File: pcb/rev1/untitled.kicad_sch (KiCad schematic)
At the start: 40 parts, among them U7 TL084, U8 TL084

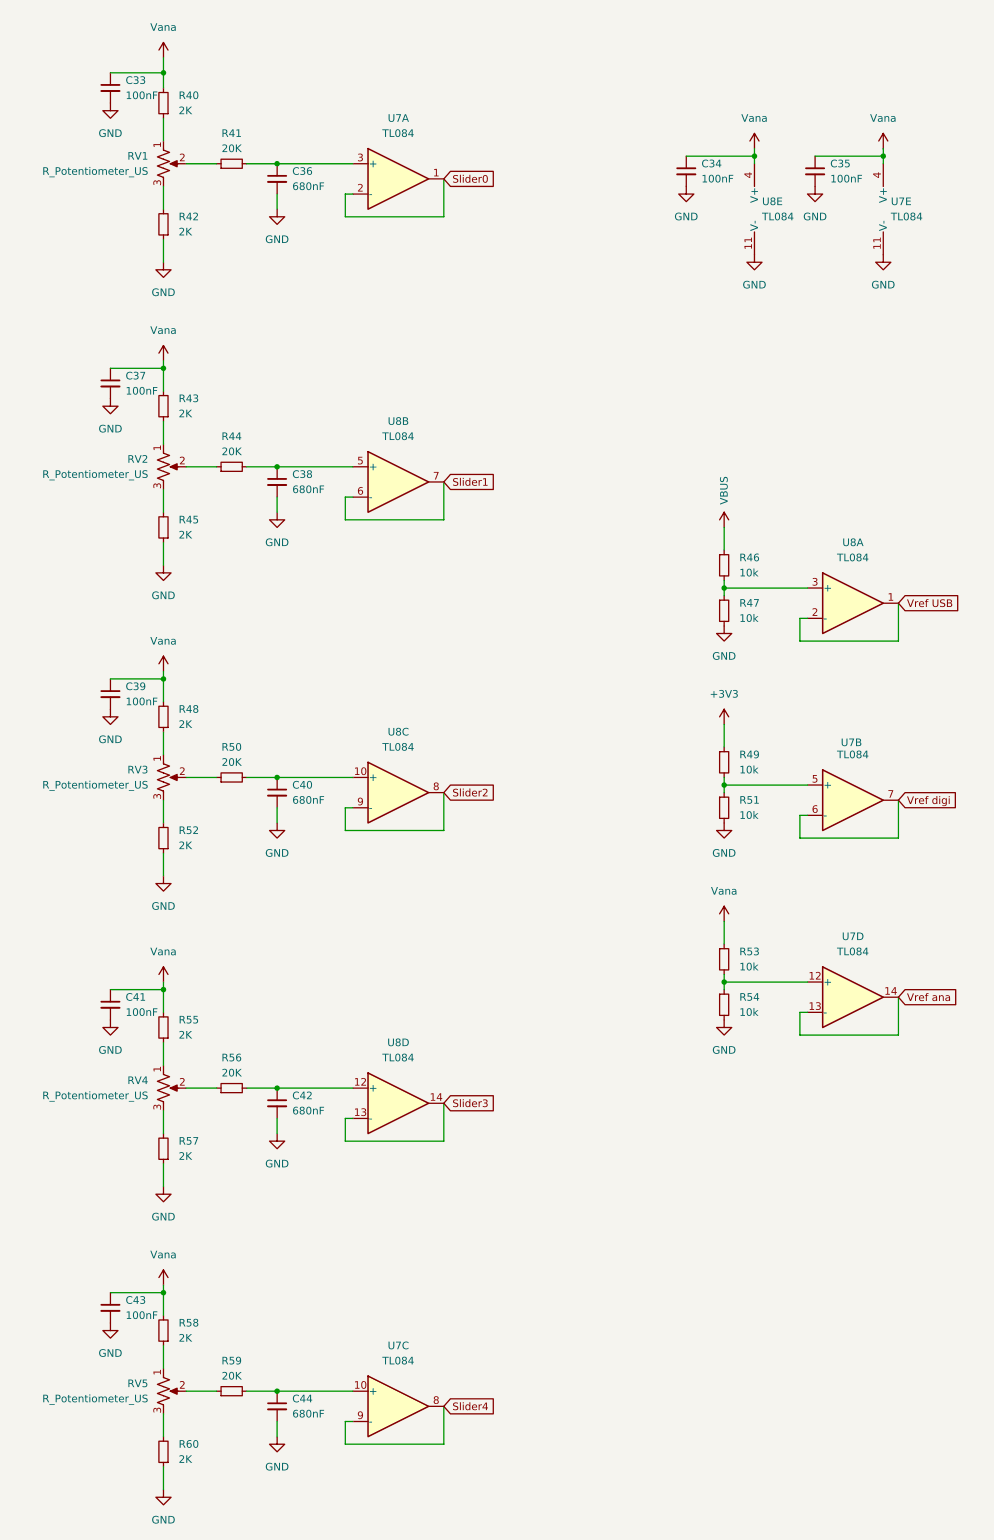
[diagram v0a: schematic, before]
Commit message: avancer du layout
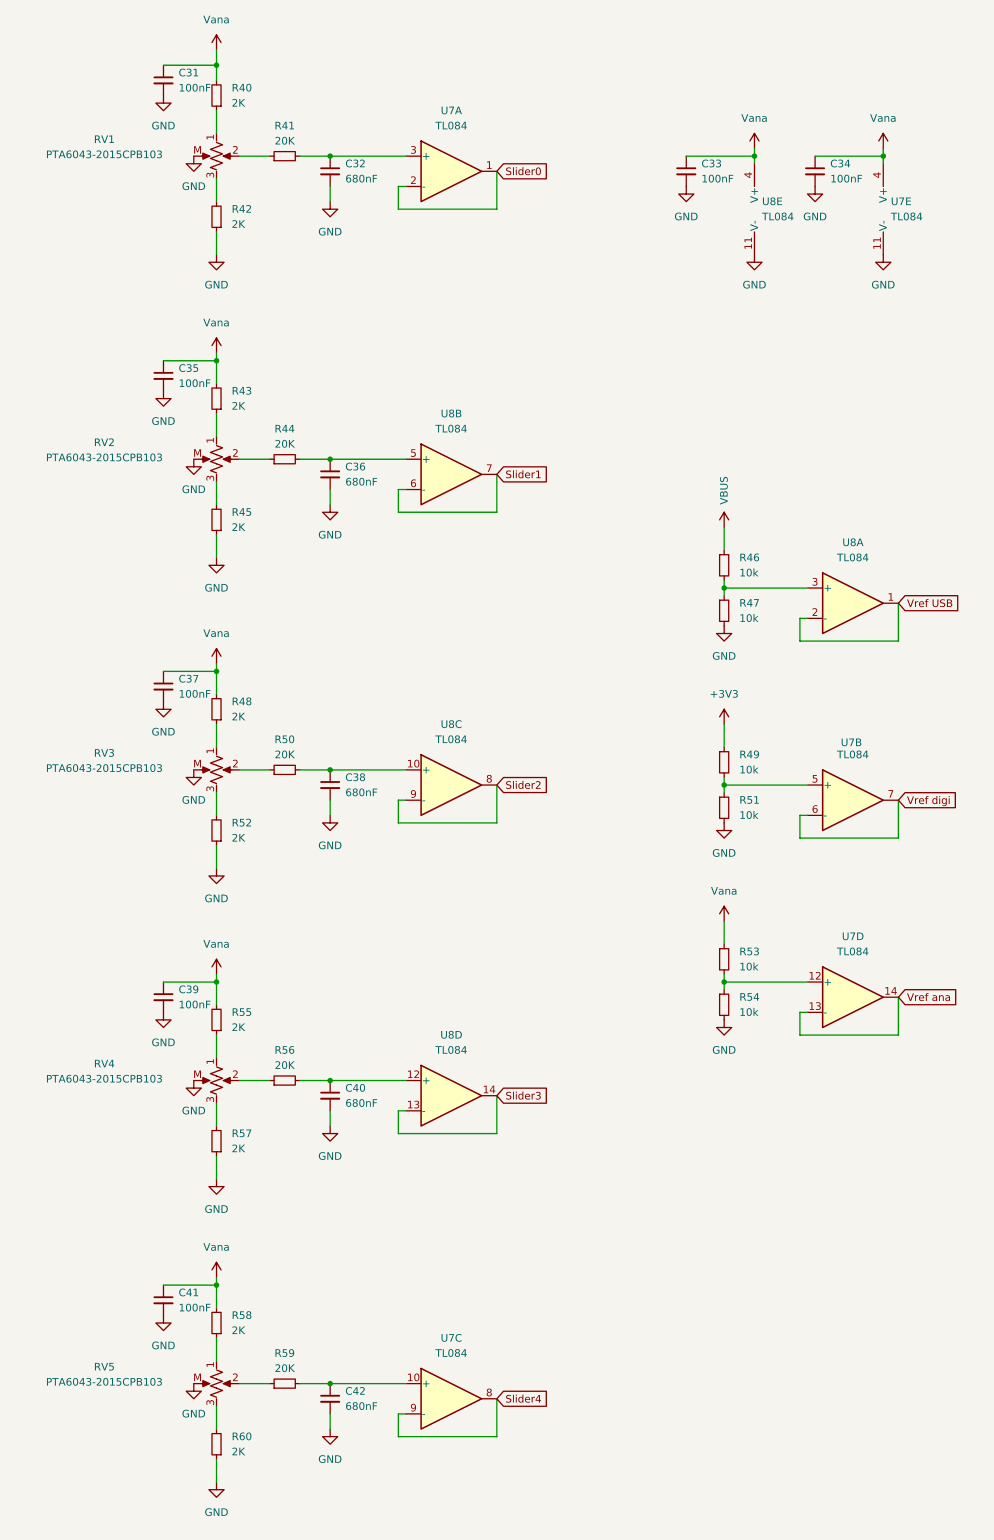
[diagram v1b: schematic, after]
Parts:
- removed RV1, RV2, RV3, RV4, RV5: R_Potentiometer_US, A_Please:Slider Bourns PTA6043-2015CPB103, symbol Device:R_Potentiometer_US
- added RV1, RV2, RV3, RV4, RV5: PTA6043-2015CPB103, A_Please:Slider Bourns PTA6043-2015CPB103, symbol Please:Slider_Bourns_PTA6043-2015CPB103
- C31: renamed from C33; footprint (none) -> Capacitor_SMD:C_0603_1608Metric
- C32: renamed from C36; footprint (none) -> Capacitor_SMD:C_0603_1608Metric
- C33: renamed from C34; footprint (none) -> Capacitor_SMD:C_0603_1608Metric
- C34: renamed from C35; footprint (none) -> Capacitor_SMD:C_0603_1608Metric
- C35: renamed from C37; footprint (none) -> Capacitor_SMD:C_0603_1608Metric
- C36: renamed from C38; footprint (none) -> Capacitor_SMD:C_0603_1608Metric
- C37: renamed from C39; footprint (none) -> Capacitor_SMD:C_0603_1608Metric
- C38: renamed from C40; footprint (none) -> Capacitor_SMD:C_0603_1608Metric
- C39: renamed from C41; footprint (none) -> Capacitor_SMD:C_0603_1608Metric
- C40: renamed from C42; footprint (none) -> Capacitor_SMD:C_0603_1608Metric
- C41: renamed from C43; footprint (none) -> Capacitor_SMD:C_0603_1608Metric
- C42: renamed from C44; footprint (none) -> Capacitor_SMD:C_0603_1608Metric
- R40, R41, R42, R43, R44, R45, R46, R47, R48, R49, R50, R51, R52, R53, R54, R55, R56, R57, R58, R59, R60: footprint (none) -> Resistor_SMD:R_0603_1608Metric
- U7, U8: footprint (none) -> Package_SO:SOIC-14_3.9x8.7mm_P1.27mm
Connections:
- net GND: now also RV1.M, RV2.M, RV3.M, RV4.M, RV5.M
- net at R44.1: now also RV2.2
- net at R48.1: now also RV3.1
- net at R50.1: now also RV3.2
- net at R52.2: now also RV3.3
- net at R43.1: now also RV2.1
- net at R56.1: now also RV4.2
- net at R42.2: now also RV1.3
- net at R40.1: now also RV1.1
- net at R41.1: now also RV1.2
- net at R57.2: now also RV4.3
- net at R59.1: now also RV5.2
- net at R58.1: now also RV5.1
- net at R60.2: now also RV5.3
- net at R55.1: now also RV4.1
- net at R45.2: now also RV2.3
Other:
- moved on the sheet: C31, C32, C35, C36, C37, C38, C39, C40, C41, C42, R40, R41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

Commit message: BIDIBOU
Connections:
- net Slider0: now also U8.1, U8.2 (-); no longer U7.1, U7.2 (-)
- net Slider4: now also U7.1, U7.2 (-); no longer U7.8, U7.9 (-)
- net Vref USB: now also U7.6 (-), U7.7; no longer U8.1, U8.2 (-)
- net Vref digi: now also U7.8, U7.9 (-); no longer U7.6 (-), U7.7
- net at R46.2, R47.1: now also U7.5 (+); no longer U8.3 (+)
- net at C42.1, R59.2: now also U7.3 (+); no longer U7.10 (+)
- net at C32.1, R41.2: now also U8.3 (+); no longer U7.3 (+)
- net at R49.2, R51.1: now also U7.10 (+); no longer U7.5 (+)
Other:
- moved on the sheet: U7A, U7B, U7C, U8A
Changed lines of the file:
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@@
 	(symbol
 		(lib_id "Amplifier_Operational:TL084")
-		(at 85.09 246.38 0)
+		(at 152.4 146.05 0)
 		(unit 3)
 		(exclude_from_sim no)
@@
 		(fields_autoplaced yes)
 		(property "Reference" "U7"
-			(at 85.09 236.22 0)
+			(at 152.4 135.89 0)
 			(effects
 				(font
@@
 		)
 		(property "Value" "TL084"
-			(at 85.09 238.76 0)
+			(at 152.4 138.43 0)
 			(effects
 				(font
@@
 		)
 		(property "Footprint" "Package_SO:SOIC-14_3.9x8.7mm_P1.27mm"
-			(at 83.82 243.84 0)
+			(at 151.13 143.51 0)
 			(effects
 				(font
@@
 		)
 		(property "Datasheet" "http://www.ti.com/lit/ds/symlink/tl081.pdf"
-			(at 86.36 241.3 0)
+			(at 153.67 140.97 0)
 			(effects
 				(font
@@
 		)
 		(property "Description" "Quad JFET-Input Operational Amplifiers, DIP-14/SOIC-14/SSOP-14"
-			(at 85.09 246.38 0)
+			(at 152.4 146.05 0)
 			(effects
 				(font
@@
 	(symbol
 		(lib_id "Amplifier_Operational:TL084")
-		(at 152.4 113.03 0)
+		(at 85.09 40.64 0)
 		(unit 1)
 		(exclude_from_sim no)
@@
 		(fields_autoplaced yes)
 		(property "Reference" "U8"
-			(at 152.4 102.87 0)
+			(at 85.09 30.48 0)
 			(effects
 				(font
@@
 		)
 		(property "Value" "TL084"
-			(at 152.4 105.41 0)
+			(at 85.09 33.02 0)
 			(effects
 				(font
@@
 		)
 		(property "Footprint" "Package_SO:SOIC-14_3.9x8.7mm_P1.27mm"
-			(at 151.13 110.49 0)
+			(at 83.82 38.1 0)
 			(effects
 				(font
@@
 		)
 		(property "Datasheet" "http://www.ti.com/lit/ds/symlink/tl081.pdf"
-			(at 153.67 107.95 0)
+			(at 86.36 35.56 0)
 			(effects
 				(font
@@
 		)
 		(property "Description" "Quad JFET-Input Operational Amplifiers, DIP-14/SOIC-14/SSOP-14"
-			(at 152.4 113.03 0)
+			(at 85.09 40.64 0)
 			(effects
 				(font
@@
 	(symbol
 		(lib_id "Amplifier_Operational:TL084")
-		(at 152.4 146.05 0)
+		(at 152.4 113.03 0)
 		(unit 2)
 		(exclude_from_sim no)
@@
 		(dnp no)
 		(property "Reference" "U7"
-			(at 152.146 136.398 0)
+			(at 152.146 103.378 0)
 			(effects
 				(font
@@
 		)
 		(property "Value" "TL084"
-			(at 152.4 138.43 0)
+			(at 152.4 105.41 0)
 			(effects
 				(font
@@
 		)
 		(property "Footprint" "Package_SO:SOIC-14_3.9x8.7mm_P1.27mm"
-			(at 151.13 143.51 0)
+			(at 151.13 110.49 0)
 			(effects
 				(font
@@
 		)
 		(property "Datasheet" "http://www.ti.com/lit/ds/symlink/tl081.pdf"
-			(at 153.67 140.97 0)
+			(at 153.67 107.95 0)
 			(effects
 				(font
@@
 		)
 		(property "Description" "Quad JFET-Input Operational Amplifiers, DIP-14/SOIC-14/SSOP-14"
-			(at 152.4 146.05 0)
+			(at 152.4 113.03 0)
 			(effects
 				(font
@@
 	(symbol
 		(lib_id "Amplifier_Operational:TL084")
-		(at 85.09 40.64 0)
+		(at 85.09 246.38 0)
 		(unit 1)
 		(exclude_from_sim no)
@@
 		(fields_autoplaced yes)
 		(property "Reference" "U7"
-			(at 85.09 30.48 0)
+			(at 85.09 236.22 0)
 			(effects
 				(font
@@
 		)
 		(property "Value" "TL084"
-			(at 85.09 33.02 0)
+			(at 85.09 238.76 0)
 			(effects
 				(font
@@
 		)
 		(property "Footprint" "Package_SO:SOIC-14_3.9x8.7mm_P1.27mm"
-			(at 83.82 38.1 0)
+			(at 83.82 243.84 0)
 			(effects
 				(font
@@
 		)
 		(property "Datasheet" "http://www.ti.com/lit/ds/symlink/tl081.pdf"
-			(at 86.36 35.56 0)
+			(at 86.36 241.3 0)
 			(effects
 				(font
@@
 		)
 		(property "Description" "Quad JFET-Input Operational Amplifiers, DIP-14/SOIC-14/SSOP-14"
-			(at 85.09 40.64 0)
+			(at 85.09 246.38 0)
 			(effects
 				(font

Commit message: BIDIBOU
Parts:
- renumbered C31 to C47, C32 to C48, C33 to C49, C34 to C50, C35 to C51, C36 to C52, C37 to C53, C38 to C54, C39 to C55, C40 to C56, C41 to C57, C42 to C58, R40 to R56, R41 to R57, R42 to R58, R43 to R59, R44 to R60, R45 to R61, R46 to R62, R47 to R63, R48 to R64, R49 to R65, R50 to R66, R51 to R67, R52 to R68, R53 to R69, R54 to R70, R55 to R71, R56 to R72, R57 to R73, R58 to R74, R59 to R75, R60 to R76, U8 to U7, U7 to U8
